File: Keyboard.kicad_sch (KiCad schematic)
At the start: 21 parts, among them J1 AVR-ISP-6, SW1 SW_Push, U1 ATmega32U4-A, U2 PRTR5V0U2X, Y1 16MHz

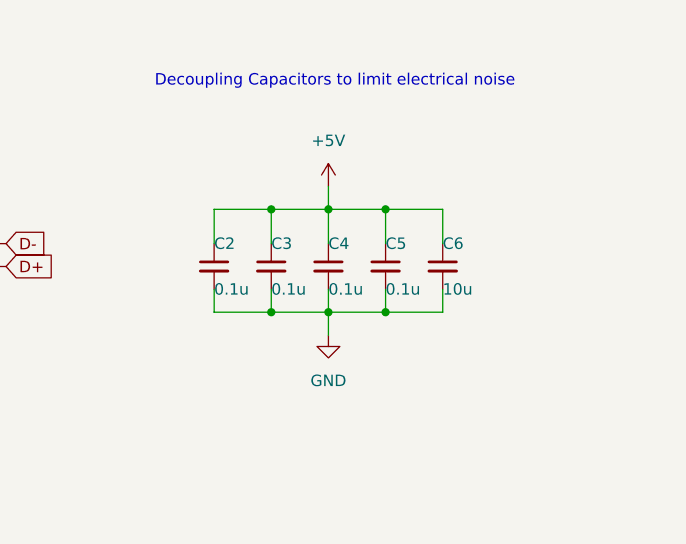
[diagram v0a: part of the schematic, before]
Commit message: Connected USB data lines and power lines to MCU
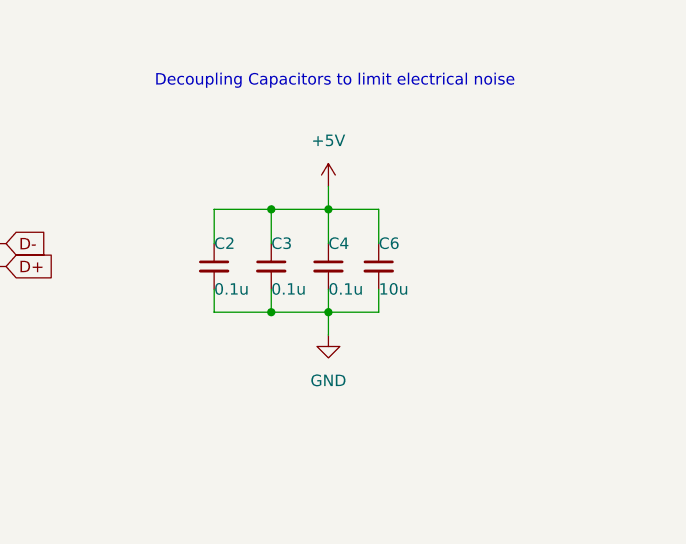
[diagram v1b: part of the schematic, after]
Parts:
- removed C5: 0.1u, Capacitor_SMD:C_0805_2012Metric_Pad1.18x1.45mm_HandSolder, symbol Device:C_Small
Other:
- moved on the sheet: C6
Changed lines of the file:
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@@
   (junction (at 244.094 46.99) (diameter 0) (color 0 0 0 0)
   )
-  (junction (at 256.794 35.56) (diameter 0) (color 0 0 0 0)
-  )
   (junction (at 250.444 46.99) (diameter 0) (color 0 0 0 0)
   )
@@
   )
   (junction (at 172.72 39.37) (diameter 0) (color 0 0 0 0)
-  )
-  (junction (at 256.794 46.99) (diameter 0) (color 0 0 0 0)
   )
   (junction (at 163.195 52.07) (diameter 0) (color 0 0 0 0)
@@
   (no_connect (at 90.17 116.84))
   (no_connect (at 90.17 104.14))
+  (wire (pts (xy 250.444 46.99) (xy 256.032 46.99))
+    (stroke (width 0) (type default) (color 0 0 0 0))
+  )
   (wire (pts (xy 26.67 38.735) (xy 31.115 38.735))
     (stroke (width 0) (type default) (color 0 0 0 0))
@@
     (stroke (width 0) (type default) (color 0 0 0 0))
   )
+  (wire (pts (xy 250.444 35.56) (xy 256.032 35.56))
+    (stroke (width 0) (type default) (color 0 0 0 0))
+  )
   (wire (pts (xy 163.195 24.13) (xy 160.02 24.13))
     (stroke (width 0) (type default) (color 0 0 0 0))
@@
     (stroke (width 0) (type default) (color 0 0 0 0))
   )
-  (wire (pts (xy 250.444 46.99) (xy 256.794 46.99))
-    (stroke (width 0) (type default) (color 0 0 0 0))
-  )
   (wire (pts (xy 117.475 25.4) (xy 117.475 29.21))
     (stroke (width 0) (type default) (color 0 0 0 0))
@@
     (stroke (width 0) (type default) (color 0 0 0 0))
   )
-  (wire (pts (xy 256.794 46.99) (xy 263.144 46.99))
-    (stroke (width 0) (type default) (color 0 0 0 0))
-  )
   (wire (pts (xy 172.085 52.07) (xy 178.435 52.07))
     (stroke (width 0) (type default) (color 0 0 0 0))
@@
     (stroke (width 0) (type default) (color 0 0 0 0))
   )
-  (wire (pts (xy 256.794 44.45) (xy 256.794 46.99))
-    (stroke (width 0) (type default) (color 0 0 0 0))
-  )
   (wire (pts (xy 117.475 36.83) (xy 117.475 39.37))
     (stroke (width 0) (type default) (color 0 0 0 0))
@@
     (stroke (width 0) (type default) (color 0 0 0 0))
   )
-  (wire (pts (xy 256.794 35.56) (xy 263.144 35.56))
-    (stroke (width 0) (type default) (color 0 0 0 0))
-  )
   (wire (pts (xy 244.094 35.56) (xy 250.444 35.56))
     (stroke (width 0) (type default) (color 0 0 0 0))
@@
     (stroke (width 0) (type default) (color 0 0 0 0))
   )
-  (wire (pts (xy 250.444 35.56) (xy 256.794 35.56))
-    (stroke (width 0) (type default) (color 0 0 0 0))
-  )
   (wire (pts (xy 163.195 52.07) (xy 163.195 24.13))
     (stroke (width 0) (type default) (color 0 0 0 0))
   )
-  (wire (pts (xy 256.794 35.56) (xy 256.794 39.37))
-    (stroke (width 0) (type default) (color 0 0 0 0))
-  )
   (wire (pts (xy 250.444 49.53) (xy 250.444 46.99))
     (stroke (width 0) (type default) (color 0 0 0 0))
   )
-  (wire (pts (xy 263.144 46.99) (xy 263.144 44.45))
+  (wire (pts (xy 256.032 46.99) (xy 256.032 44.45))
     (stroke (width 0) (type default) (color 0 0 0 0))
   )
@@
     (stroke (width 0) (type default) (color 0 0 0 0))
   )
-  (wire (pts (xy 263.144 35.56) (xy 263.144 39.37))
+  (wire (pts (xy 256.032 35.56) (xy 256.032 39.37))
     (stroke (width 0) (type default) (color 0 0 0 0))
   )
@@
     (pin "1")
   )
-  (symbol (lib_id "Device:C_Small") (at 256.794 41.91 0) (unit 1)
-    (in_bom yes) (on_board yes)
-    (property "Reference" "C5" (id 0) (at 256.794 39.37 0)
-      (effects (font (size 1.27 1.27)) (justify left))
-    )
-    (property "Value" "0.1u" (id 1) (at 256.794 44.45 0)
-      (effects (font (size 1.27 1.27)) (justify left))
-    )
-    (property "Footprint" "Capacitor_SMD:C_0805_2012Metric_Pad1.18x1.45mm_HandSolder" (id 2) (at 256.794 41.91 0)
-      (effects (font (size 1.27 1.27)) hide)
-    )
-    (property "Datasheet" "~" (id 3) (at 256.794 41.91 0)
-      (effects (font (size 1.27 1.27)) hide)
-    )
-    (pin "1")
-    (pin "2")
-  )
   (symbol (lib_id "power:+5V") (at 250.444 33.02 0) (unit 1)
     (in_bom yes) (on_board yes) (fields_autoplaced)
@@
     (pin "1")
   )
-  (symbol (lib_id "Device:C_Small") (at 263.144 41.91 0) (unit 1)
-    (in_bom yes) (on_board yes)
-    (property "Reference" "C6" (id 0) (at 263.144 39.37 0)
-      (effects (font (size 1.27 1.27)) (justify left))
-    )
-    (property "Value" "10u" (id 1) (at 263.144 44.45 0)
-      (effects (font (size 1.27 1.27)) (justify left))
-    )
-    (property "Footprint" "Capacitor_SMD:C_0805_2012Metric_Pad1.18x1.45mm_HandSolder" (id 2) (at 263.144 41.91 0)
-      (effects (font (size 1.27 1.27)) hide)
-    )
-    (property "Datasheet" "~" (id 3) (at 263.144 41.91 0)
+  (symbol (lib_id "Device:C_Small") (at 256.032 41.91 0) (unit 1)
+    (in_bom yes) (on_board yes)
+    (property "Reference" "C6" (id 0) (at 256.032 39.37 0)
+      (effects (font (size 1.27 1.27)) (justify left))
+    )
+    (property "Value" "10u" (id 1) (at 256.032 44.45 0)
+      (effects (font (size 1.27 1.27)) (justify left))
+    )
+    (property "Footprint" "Capacitor_SMD:C_0805_2012Metric_Pad1.18x1.45mm_HandSolder" (id 2) (at 256.032 41.91 0)
+      (effects (font (size 1.27 1.27)) hide)
+    )
+    (property "Datasheet" "~" (id 3) (at 256.032 41.91 0)
       (effects (font (size 1.27 1.27)) hide)
     )
@@
       (reference "C4") (unit 1) (value "0.1u") (footprint "Capacitor_SMD:C_0805_2012Metric_Pad1.18x1.45mm_HandSolder")
     )
-    (path "/8a6bdb1a-e565-4322-a9ce-3d54b2bde084"
-      (reference "C5") (unit 1) (value "0.1u") (footprint "Capacitor_SMD:C_0805_2012Metric_Pad1.18x1.45mm_HandSolder")
-    )
     (path "/98b09405-43ad-40e6-a731-841c6ea28b01"

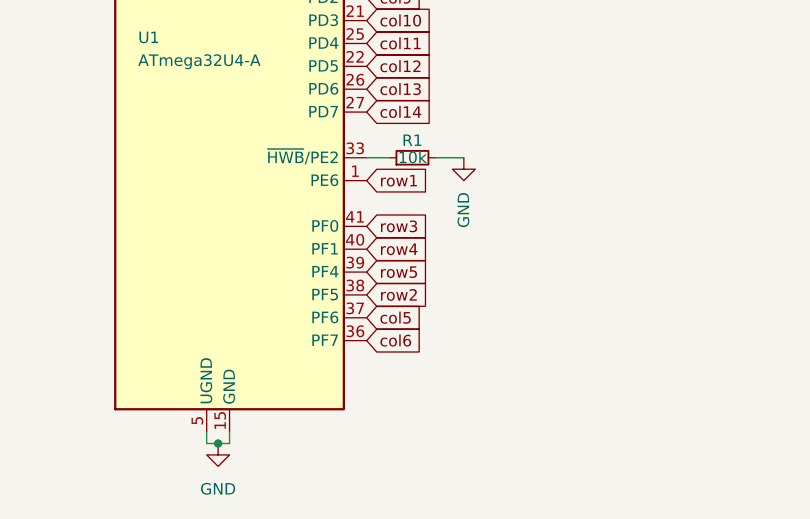
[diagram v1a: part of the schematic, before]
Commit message: Added buses for like tracks and changed 5V track layout
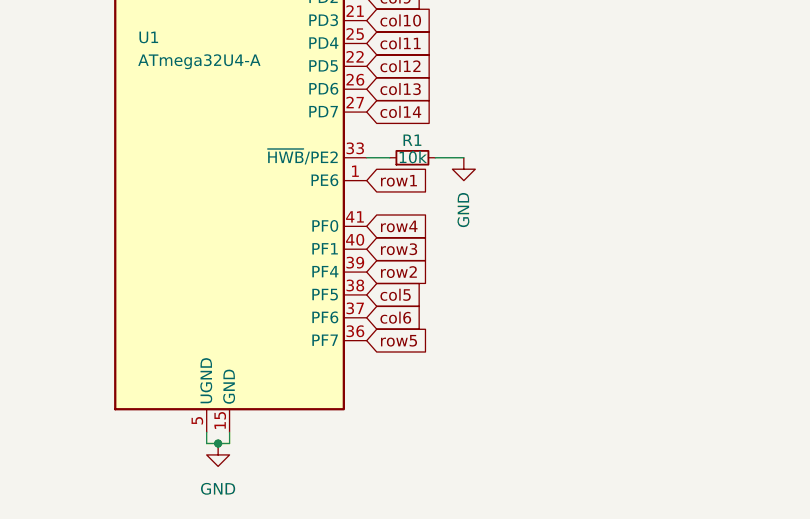
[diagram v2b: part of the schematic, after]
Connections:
- net col5: now also U1.38 (PF5); no longer U1.37 (PF6)
- net col6: now also U1.37 (PF6); no longer U1.36 (PF7)
- net row2: now also U1.39 (PF4); no longer U1.38 (PF5)
- net row3: now also U1.40 (PF1); no longer U1.41 (PF0)
- net row4: now also U1.41 (PF0); no longer U1.40 (PF1)
- net row5: now also U1.36 (PF7); no longer U1.39 (PF4)

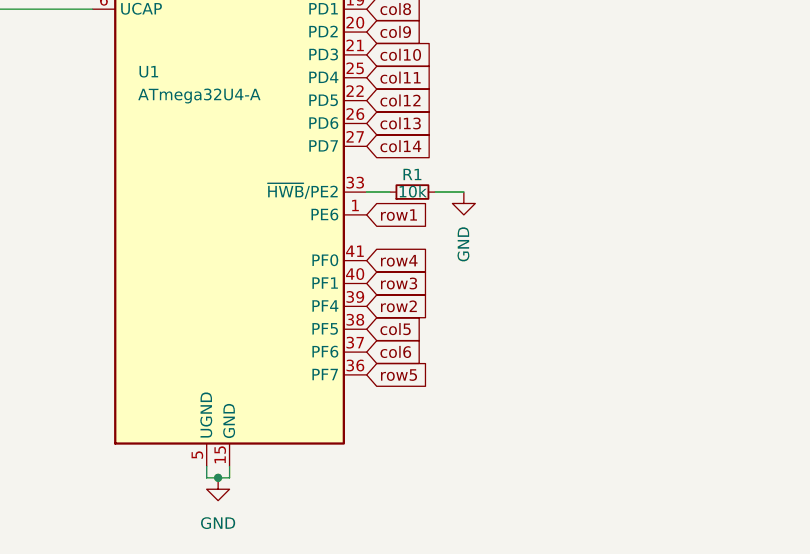
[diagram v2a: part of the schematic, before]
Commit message: Connected all columns and rows to MCU and removed redundant vias
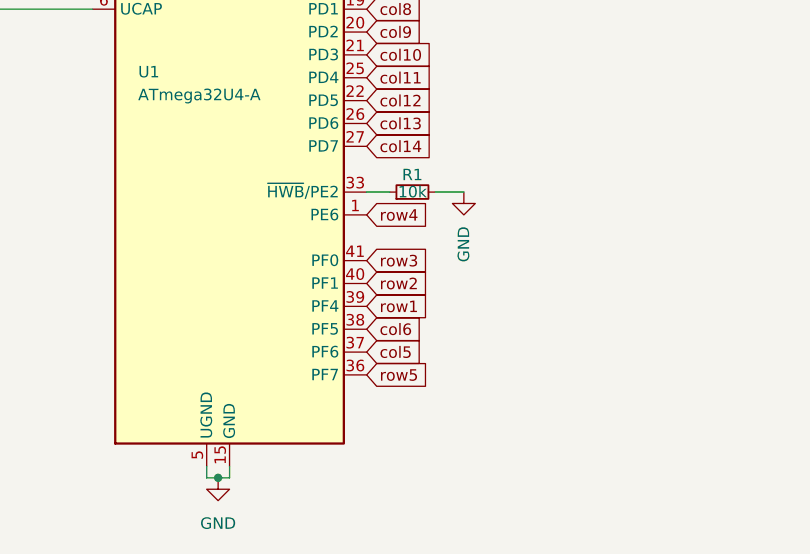
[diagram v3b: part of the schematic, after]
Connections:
- net col5: now also U1.37 (PF6); no longer U1.38 (PF5)
- net col6: now also U1.38 (PF5); no longer U1.37 (PF6)
- net row1: now also U1.39 (PF4); no longer U1.1 (PE6)
- net row2: now also U1.40 (PF1); no longer U1.39 (PF4)
- net row3: now also U1.41 (PF0); no longer U1.40 (PF1)
- net row4: now also U1.1 (PE6); no longer U1.41 (PF0)

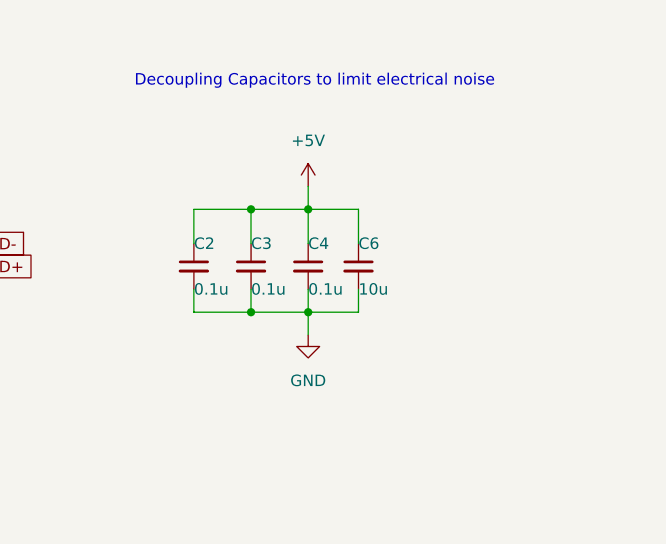
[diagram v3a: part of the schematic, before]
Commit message: Connected reset button and ISP header to MCU, added ground pour on B.Cu, and updated footprints
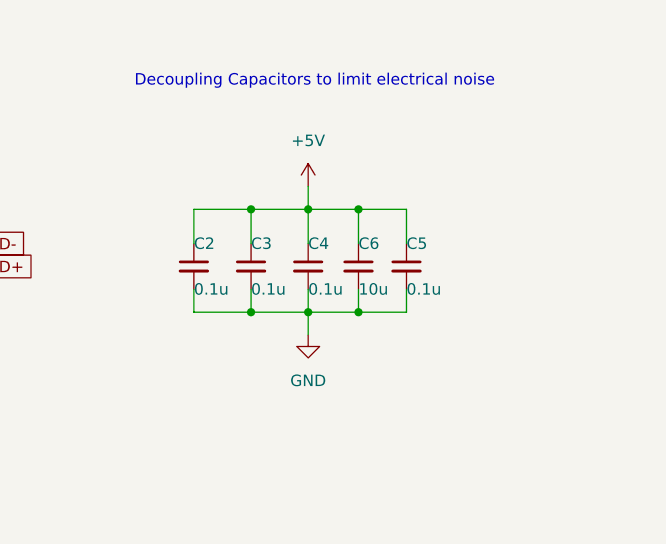
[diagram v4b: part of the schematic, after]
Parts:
- added C5: 0.1u, Capacitor_SMD:C_0805_2012Metric_Pad1.18x1.45mm_HandSolder, symbol Device:C_Small
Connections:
- net +5V: now also C5.1
- net GND: now also C5.2
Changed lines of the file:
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@@
     (rev "0")
   )
+  (junction (at 256.032 46.99) (diameter 0) (color 0 0 0 0)
+  )
   (junction (at 165.735 26.67) (diameter 0) (color 0 0 0 0)
   )
@@
   )
   (junction (at 187.96 26.67) (diameter 0) (color 0 0 0 0)
+  )
+  (junction (at 256.032 35.56) (diameter 0) (color 0 0 0 0)
   )
   (junction (at 26.67 41.91) (diameter 0) (color 0 0 0 0)
@@
     (stroke (width 0) (type default) (color 0 0 0 0))
   )
+  (wire (pts (xy 256.032 46.99) (xy 261.366 46.99))
+    (stroke (width 0) (type default) (color 0 0 0 0))
+  )
   (wire (pts (xy 165.735 52.07) (xy 172.085 52.07))
     (stroke (width 0) (type default) (color 0 0 0 0))
@@
     (stroke (width 0) (type default) (color 0 0 0 0))
   )
+  (wire (pts (xy 256.032 35.56) (xy 261.366 35.56))
+    (stroke (width 0) (type default) (color 0 0 0 0))
+  )
   (wire (pts (xy 160.02 36.83) (xy 174.625 36.83))
     (stroke (width 0) (type default) (color 0 0 0 0))
@@
     (stroke (width 0) (type default) (color 0 0 0 0))
   )
+  (wire (pts (xy 261.366 46.99) (xy 261.366 44.45))
+    (stroke (width 0) (type default) (color 0 0 0 0))
+  )
   (wire (pts (xy 19.05 34.29) (xy 19.05 35.56))
     (stroke (width 0) (type default) (color 0 0 0 0))
@@
   )
   (wire (pts (xy 77.47 78.74) (xy 77.47 76.835))
+    (stroke (width 0) (type default) (color 0 0 0 0))
+  )
+  (wire (pts (xy 261.366 35.56) (xy 261.366 39.37))
     (stroke (width 0) (type default) (color 0 0 0 0))
   )
@@
     (pin "1")
   )
+  (symbol (lib_id "Device:C_Small") (at 261.366 41.91 0) (unit 1)
+    (in_bom yes) (on_board yes)
+    (property "Reference" "C5" (id 0) (at 261.366 39.37 0)
+      (effects (font (size 1.27 1.27)) (justify left))
+    )
+    (property "Value" "0.1u" (id 1) (at 261.366 44.45 0)
+      (effects (font (size 1.27 1.27)) (justify left))
+    )
+    (property "Footprint" "Capacitor_SMD:C_0805_2012Metric_Pad1.18x1.45mm_HandSolder" (id 2) (at 261.366 41.91 0)
+      (effects (font (size 1.27 1.27)) hide)
+    )
+    (property "Datasheet" "~" (id 3) (at 261.366 41.91 0)
+      (effects (font (size 1.27 1.27)) hide)
+    )
+    (pin "1")
+    (pin "2")
+  )
   (symbol (lib_id "Device:R_Small") (at 178.435 49.53 0) (unit 1)
     (in_bom yes) (on_board yes)
@@
       (reference "C4") (unit 1) (value "0.1u") (footprint "Capacitor_SMD:C_0805_2012Metric_Pad1.18x1.45mm_HandSolder")
     )
+    (path "/f33b6101-b074-498f-ba05-c07f5dfdd7a2"
+      (reference "C5") (unit 1) (value "0.1u") (footprint "Capacitor_SMD:C_0805_2012Metric_Pad1.18x1.45mm_HandSolder")
+    )
     (path "/98b09405-43ad-40e6-a731-841c6ea28b01"

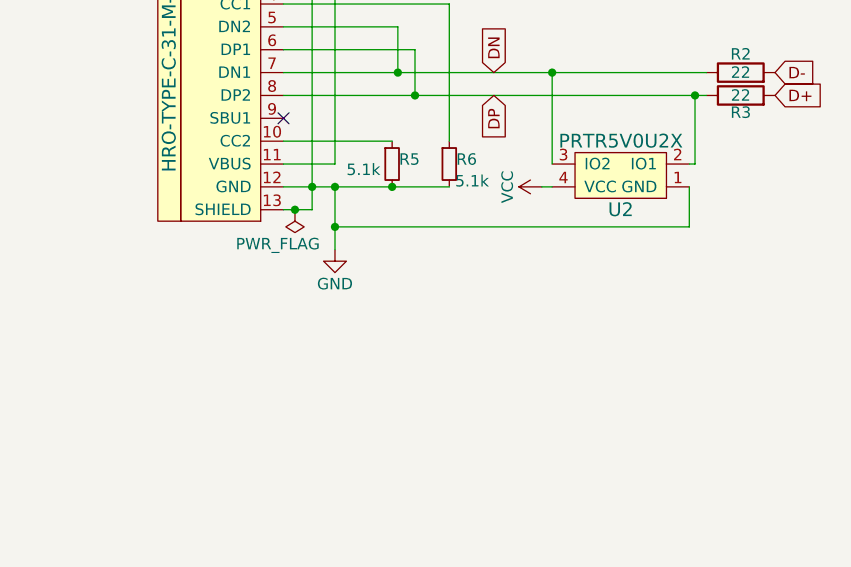
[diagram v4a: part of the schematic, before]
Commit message: Added ferrite bead to prevent ESDs
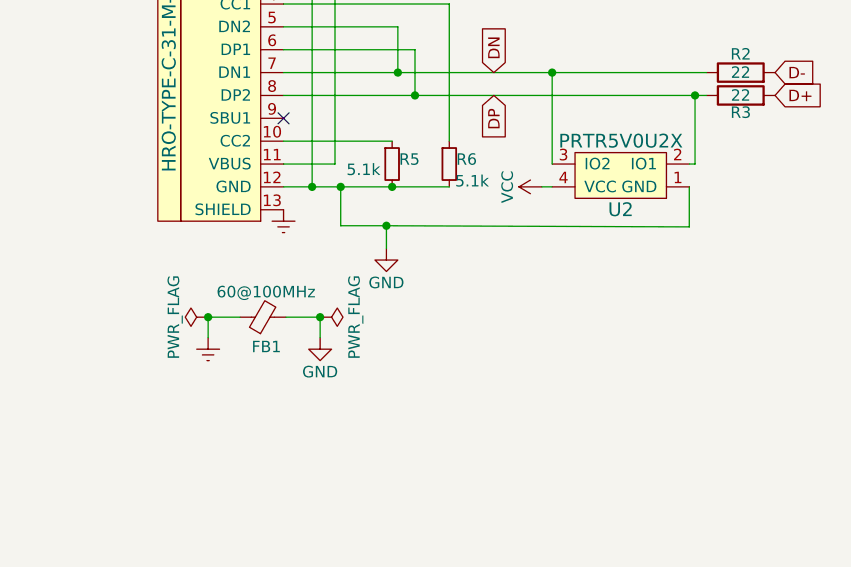
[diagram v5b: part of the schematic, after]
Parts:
- added FB1: 60@100MHz, Inductor_SMD:L_0805_2012Metric_Pad1.15x1.40mm_HandSolder, symbol Device:FerriteBead_Small
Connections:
- net GND: now also FB1.2; no longer USB1.13 (SHIELD)
- new net Earth: FB1.1, USB1.13 (SHIELD)
